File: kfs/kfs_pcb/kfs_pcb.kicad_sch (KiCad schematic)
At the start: 76 parts, among them SW0 SWITCH, SW1 SWITCH, SW10 SWITCH, SW11 SWITCH, SW12 SWITCH, SW13 SWITCH, SW14 SWITCH, SW15 SWITCH, SW16 SWITCH, SW17 SWITCH, SW18 SWITCH, SW19 SWITCH, SW2 SWITCH, SW20 SWITCH, SW21 SWITCH, SW22 SWITCH, SW23 SWITCH, SW24 SWITCH, SW25 SWITCH, SW26 SWITCH, SW27 SWITCH, SW28 SWITCH, SW29 SWITCH, SW3 SWITCH, SW30 SWITCH, SW31 SWITCH, SW32 SWITCH, SW33 SWITCH, SW34 SWITCH, SW35 SWITCH, SW36 SWITCH, SW37 SWITCH, SW38 SWITCH, SW39 SWITCH, SW4 SWITCH, SW40 SWITCH, SW41 SWITCH, SW42 SWITCH, SW43 SWITCH, SW44 SWITCH, SW45 SWITCH, SW46 SWITCH, SW47 SWITCH, SW48 SWITCH, SW49 SWITCH, SW5 SWITCH, SW50 SWITCH, SW51 SWITCH, SW52 SWITCH, SW53 SWITCH, SW54 SWITCH, SW55 SWITCH, SW56 SWITCH, SW57 SWITCH, SW58 SWITCH, SW59 SWITCH, SW6 SWITCH, SW60 SWITCH, SW61 SWITCH, SW62 SWITCH, SW63 SWITCH, SW7 SWITCH, SW8 SWITCH, SW9 SWITCH, U0 ARDUINO_PRO_MICRO

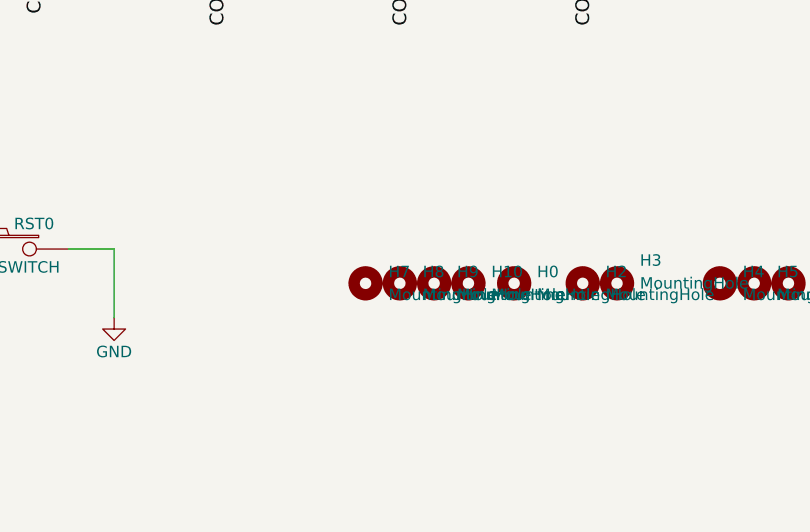
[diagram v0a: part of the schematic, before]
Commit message: Moved the bottom row of kfs farther inward.
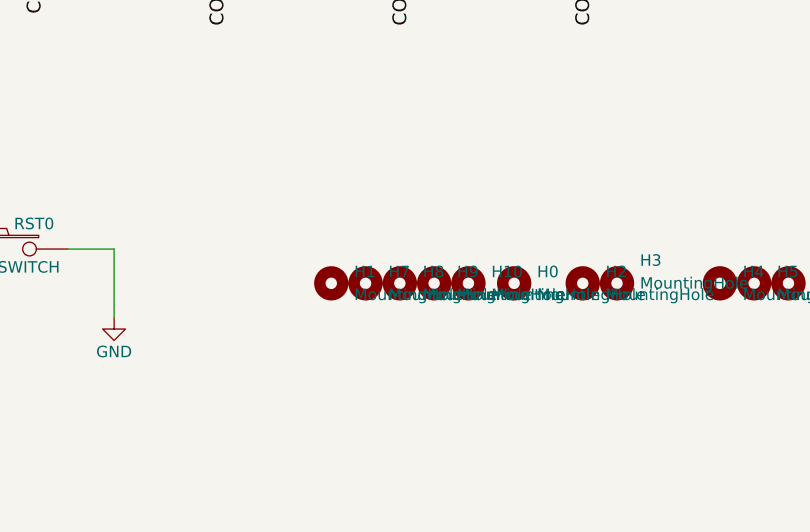
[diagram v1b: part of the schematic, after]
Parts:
- added H1: MountingHole, MountingHole:MountingHole_3.5mm, symbol Mechanical:MountingHole
- U0: footprint ProMicro_v2 -> footprints:ARDUINO_PRO_MICRO
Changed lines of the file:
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@@
       (effects (font (size 1.524 1.524)))
     )
-    (property "Footprint" "ProMicro_v2" (at 182.88 190.5 0)
+    (property "Footprint" "footprints:ARDUINO_PRO_MICRO" (at 182.88 190.5 0)
       (effects (font (size 1.524 1.524)) hide)
     )
@@
         )
       )
+    )
+  )
+  (symbol (lib_id "Mechanical:MountingHole") (at 250.19 153.67 0) (unit 1)
+    (in_bom yes) (on_board yes) (dnp no) (fields_autoplaced)
+    (property "Reference" "H1" (at 252.73 152.4 0)
+      (effects (font (size 1.27 1.27)) (justify left))
+    )
+    (property "Value" "MountingHole" (at 252.73 154.94 0)
+      (effects (font (size 1.27 1.27)) (justify left))
+    )
+    (property "Footprint" "MountingHole:MountingHole_3.5mm" (at 250.19 153.67 0)
+      (effects (font (size 1.27 1.27)) hide)
+    )
+    (property "Datasheet" "~" (at 250.19 153.67 0)
+      (effects (font (size 1.27 1.27)) hide)
+    )
+    (instances
+      (project "kfs_pcb"
+        (path "/97127b28-60f4-45ff-835e-dccfbc833331"
+          (reference "H1") (unit 1)
+        )
+      )

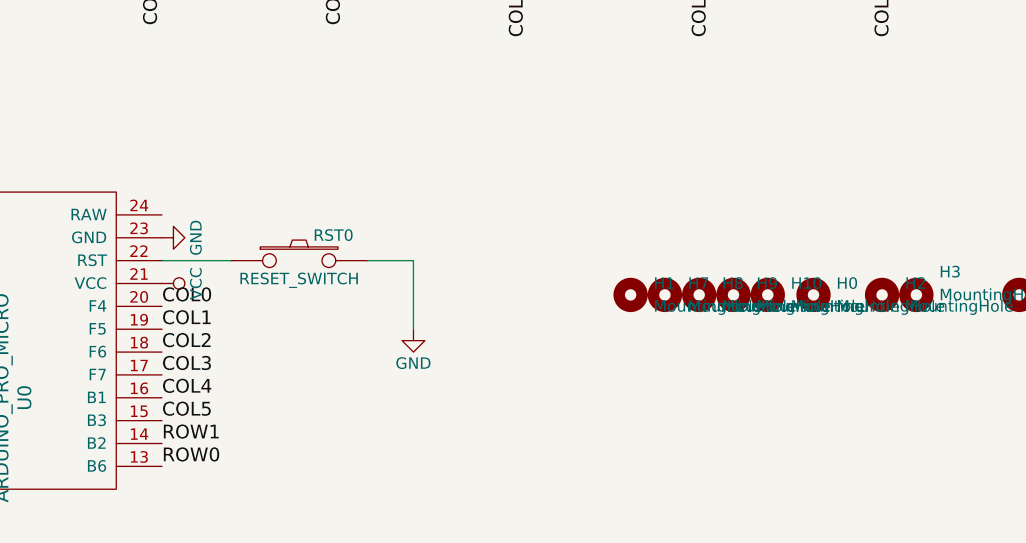
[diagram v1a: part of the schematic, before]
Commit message: Updated reset button and mounting holes on kfs.
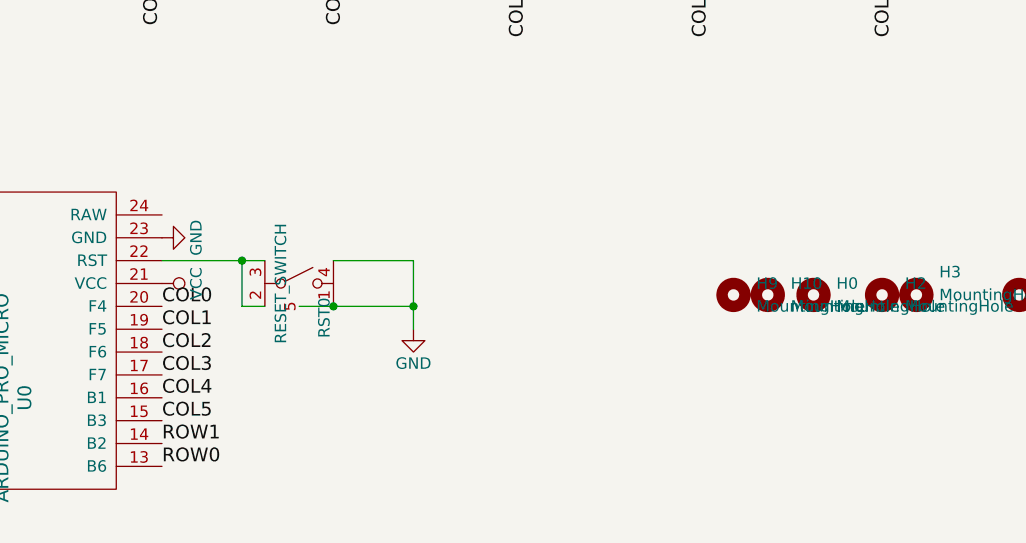
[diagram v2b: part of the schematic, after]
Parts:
- removed H1, H7, H8: MountingHole, MountingHole:MountingHole_3.5mm, symbol Mechanical:MountingHole
- RST0: footprint footprints:reset_button -> footprints:reset_button_1; symbol symbols:SWITCH_PUSH -> symbols:RESET_BUTTON
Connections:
- net GND: now also RST0.1, RST0.4, RST0.5; no longer RST0.2
- net at U0.22 (RST): now also RST0.2, RST0.3; no longer RST0.1
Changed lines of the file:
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@@
   (junction (at 193.04 35.56) (diameter 0) (color 0 0 0 0)
   )
+  (junction (at 217.17 154.94) (diameter 0) (color 0 0 0 0)
+  )
   (junction (at 91.44 92.71) (diameter 0) (color 0 0 0 0)
   )
@@
   (junction (at 152.4 111.76) (diameter 0) (color 0 0 0 0)
   )
+  (junction (at 207.01 149.86) (diameter 0) (color 0 0 0 0)
+  )
+  (junction (at 226.06 154.94) (diameter 0) (color 0 0 0 0)
+  )
   (junction (at 111.76 35.56) (diameter 0) (color 0 0 0 0)
   )
@@
     (stroke (width 0) (type default))
   )
+  (wire (pts (xy 226.06 154.94) (xy 226.06 157.48))
+    (stroke (width 0) (type default))
+  )
   (wire (pts (xy 55.88 27.94) (xy 55.88 46.99))
     (stroke (width 0) (type default))
@@
     (stroke (width 0) (type default))
   )
+  (wire (pts (xy 207.01 149.86) (xy 209.55 149.86))
+    (stroke (width 0) (type default))
+  )
   (wire (pts (xy 238.76 27.94) (xy 238.76 46.99))
     (stroke (width 0) (type default))
@@
     (stroke (width 0) (type default))
   )
-  (wire (pts (xy 226.06 149.86) (xy 226.06 157.48))
-    (stroke (width 0) (type default))
-  )
   (wire (pts (xy 152.4 35.56) (xy 172.72 35.56))
     (stroke (width 0) (type default))
@@
     (stroke (width 0) (type default))
   )
+  (wire (pts (xy 213.36 154.94) (xy 217.17 154.94))
+    (stroke (width 0) (type default))
+  )
   (wire (pts (xy 172.72 73.66) (xy 193.04 73.66))
     (stroke (width 0) (type default))
   )
+  (wire (pts (xy 209.55 154.94) (xy 207.01 154.94))
+    (stroke (width 0) (type default))
+  )
   (wire (pts (xy 238.76 85.09) (xy 238.76 104.14))
     (stroke (width 0) (type default))
   )
-  (wire (pts (xy 220.98 149.86) (xy 226.06 149.86))
+  (wire (pts (xy 217.17 149.86) (xy 226.06 149.86))
     (stroke (width 0) (type default))
   )
@@
     (stroke (width 0) (type default))
   )
-  (wire (pts (xy 198.12 149.86) (xy 205.74 149.86))
-    (stroke (width 0) (type default))
-  )
   (wire (pts (xy 254 111.76) (xy 274.32 111.76))
     (stroke (width 0) (type default))
@@
     (stroke (width 0) (type default))
   )
+  (wire (pts (xy 207.01 154.94) (xy 207.01 149.86))
+    (stroke (width 0) (type default))
+  )
   (wire (pts (xy 157.48 27.94) (xy 157.48 46.99))
     (stroke (width 0) (type default))
@@
     (stroke (width 0) (type default))
   )
+  (wire (pts (xy 217.17 154.94) (xy 226.06 154.94))
+    (stroke (width 0) (type default))
+  )
   (wire (pts (xy 111.76 54.61) (xy 132.08 54.61))
     (stroke (width 0) (type default))
@@
     (stroke (width 0) (type default))
   )
+  (wire (pts (xy 198.12 149.86) (xy 207.01 149.86))
+    (stroke (width 0) (type default))
+  )
   (wire (pts (xy 238.76 66.04) (xy 238.76 85.09))
     (stroke (width 0) (type default))
@@
   )
   (wire (pts (xy 193.04 54.61) (xy 213.36 54.61))
+    (stroke (width 0) (type default))
+  )
+  (wire (pts (xy 226.06 149.86) (xy 226.06 154.94))
     (stroke (width 0) (type default))
   )
@@
     )
   )
-  (symbol (lib_id "symbols:SWITCH_PUSH") (at 213.36 149.86 0) (unit 1)
+  (symbol (lib_id "symbols:RESET_BUTTON") (at 213.36 152.4 270) (unit 1)
     (in_bom yes) (on_board yes) (dnp no)
-    (property "Reference" "RST0" (at 217.17 147.066 0)
-      (effects (font (size 1.27 1.27)))
-    )
-    (property "Value" "RESET_SWITCH" (at 213.36 151.892 0)
-      (effects (font (size 1.27 1.27)))
-    )
-    (property "Footprint" "footprints:reset_button" (at 213.36 149.86 0)
-      (effects (font (size 1.524 1.524)) hide)
-    )
-    (property "Datasheet" "" (at 213.36 149.86 0)
-      (effects (font (size 1.524 1.524)) hide)
-    )
-    (pin "1")
-    (pin "2")
+    (property "Reference" "RST0" (at 216.154 156.21 0)
+      (effects (font (size 1.27 1.27)))
+    )
+    (property "Value" "RESET_SWITCH" (at 211.328 152.4 0)
+      (effects (font (size 1.27 1.27)))
+    )
+    (property "Footprint" "footprints:reset_button_1" (at 213.36 152.4 90)
+      (effects (font (size 1.27 1.27)) hide)
+    )
+    (property "Datasheet" "" (at 213.36 152.4 90)
+      (effects (font (size 1.27 1.27)) hide)
+    )
+    (pin "1")
+    (pin "2")
+    (pin "4")
+    (pin "5")
+    (pin "3")
     (instances
       (project "kfs_pcb"
@@
     )
   )
-  (symbol (lib_id "Mechanical:MountingHole") (at 250.19 153.67 0) (unit 1)
-    (in_bom yes) (on_board yes) (dnp no) (fields_autoplaced)
-    (property "Reference" "H1" (at 252.73 152.4 0)
-      (effects (font (size 1.27 1.27)) (justify left))
-    )
-    (property "Value" "MountingHole" (at 252.73 154.94 0)
-      (effects (font (size 1.27 1.27)) (justify left))
-    )
-    (property "Footprint" "MountingHole:MountingHole_3.5mm" (at 250.19 153.67 0)
-      (effects (font (size 1.27 1.27)) hide)
-    )
-    (property "Datasheet" "~" (at 250.19 153.67 0)
-      (effects (font (size 1.27 1.27)) hide)
-    )
-    (instances
-      (project "kfs_pcb"
-        (path "/97127b28-60f4-45ff-835e-dccfbc833331"
-          (reference "H1") (unit 1)
-        )
-      )
-    )
-  )
   (symbol (lib_id "symbols:SWITCH_WITH_DIODE") (at 226.06 66.04 0) (unit 1)
     (in_bom yes) (on_board yes) (dnp no) (fields_autoplaced)
@@
     )
   )
-  (symbol (lib_id "Mechanical:MountingHole") (at 254 153.67 0) (unit 1)
-    (in_bom yes) (on_board yes) (dnp no) (fields_autoplaced)
-    (property "Reference" "H7" (at 256.54 152.4 0)
-      (effects (font (size 1.27 1.27)) (justify left))
-    )
-    (property "Value" "MountingHole" (at 256.54 154.94 0)
-      (effects (font (size 1.27 1.27)) (justify left))
-    )
-    (property "Footprint" "MountingHole:MountingHole_3.5mm" (at 254 153.67 0)
-      (effects (font (size 1.27 1.27)) hide)
-    )
-    (property "Datasheet" "~" (at 254 153.67 0)
-      (effects (font (size 1.27 1.27)) hide)
-    )
-    (instances
-      (project "kfs_pcb"
-        (path "/97127b28-60f4-45ff-835e-dccfbc833331"
-          (reference "H7") (unit 1)
-        )
-      )
-    )
-  )
   (symbol (lib_id "symbols:SWITCH_WITH_DIODE") (at 226.06 46.99 0) (unit 1)
     (in_bom yes) (on_board yes) (dnp no) (fields_autoplaced)
@@
         )
       )
-    )
-  )
-  (symbol (lib_id "Mechanical:MountingHole") (at 257.81 153.67 0) (unit 1)
-    (in_bom yes) (on_board yes) (dnp no) (fields_autoplaced)
-    (property "Reference" "H8" (at 260.35 152.4 0)
-      (effects (font (size 1.27 1.27)) (justify left))
-    )
-    (property "Value" "MountingHole" (at 260.35 154.94 0)
-      (effects (font (size 1.27 1.27)) (justify left))
-    )
-    (property "Footprint" "MountingHole:MountingHole_3.5mm" (at 257.81 153.67 0)
-      (effects (font (size 1.27 1.27)) hide)
-    )
-    (property "Datasheet" "~" (at 257.81 153.67 0)
-      (effects (font (size 1.27 1.27)) hide)
-    )
-    (instances
-      (project "kfs_pcb"
-        (path "/97127b28-60f4-45ff-835e-dccfbc833331"
-          (reference "H8") (unit 1)
-        )
-      )

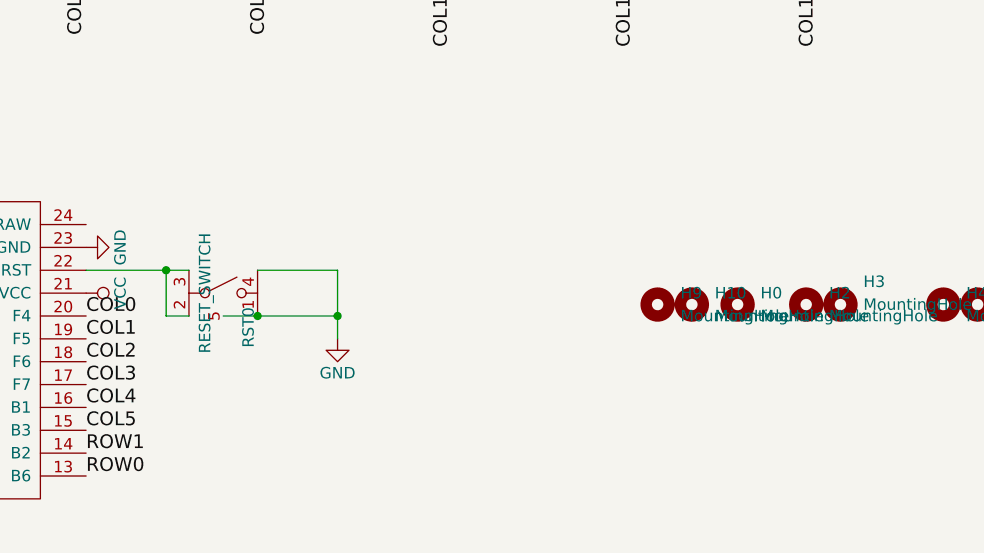
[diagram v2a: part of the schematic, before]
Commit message: Changed reset button again. Removed some standoffs.
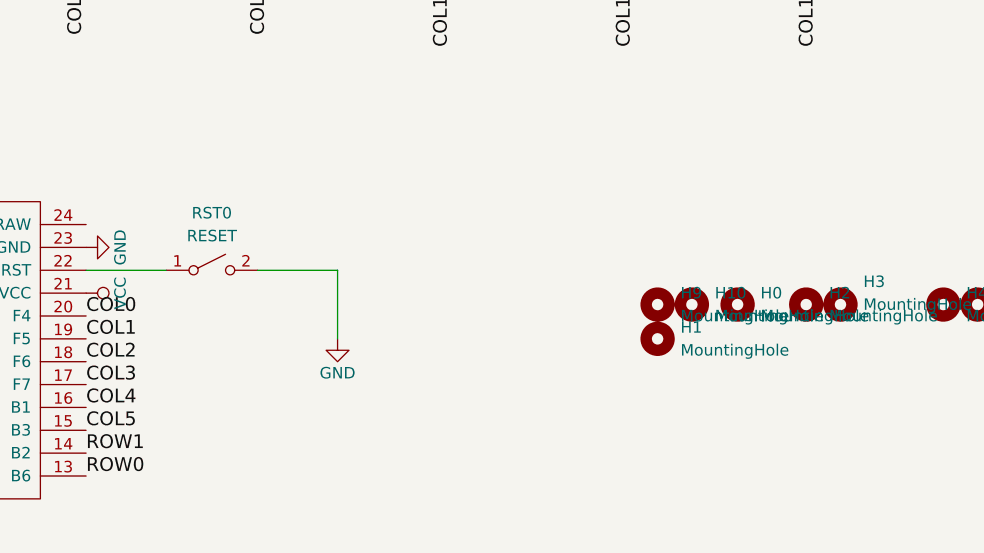
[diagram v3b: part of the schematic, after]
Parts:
- removed RST0: RESET_SWITCH, footprints:reset_button_1, symbol symbols:RESET_BUTTON
- added H1: MountingHole, MountingHole:MountingHole_3.5mm, symbol Mechanical:MountingHole
- added RST0: RESET, footprints:reset_button_1, symbol Switch:SW_SPST
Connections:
- net GND: now also RST0.2 (B)
- net at U0.22 (RST): now also RST0.1 (A)
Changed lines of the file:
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@@
   (junction (at 193.04 35.56) (diameter 0) (color 0 0 0 0)
   )
-  (junction (at 217.17 154.94) (diameter 0) (color 0 0 0 0)
-  )
   (junction (at 91.44 92.71) (diameter 0) (color 0 0 0 0)
   )
@@
   (junction (at 152.4 111.76) (diameter 0) (color 0 0 0 0)
   )
-  (junction (at 207.01 149.86) (diameter 0) (color 0 0 0 0)
-  )
-  (junction (at 226.06 154.94) (diameter 0) (color 0 0 0 0)
-  )
   (junction (at 111.76 35.56) (diameter 0) (color 0 0 0 0)
   )
@@
     (stroke (width 0) (type default))
   )
-  (wire (pts (xy 226.06 154.94) (xy 226.06 157.48))
+  (wire (pts (xy 226.06 149.86) (xy 226.06 157.48))
     (stroke (width 0) (type default))
   )
@@
     (stroke (width 0) (type default))
   )
-  (wire (pts (xy 207.01 149.86) (xy 209.55 149.86))
-    (stroke (width 0) (type default))
-  )
   (wire (pts (xy 238.76 27.94) (xy 238.76 46.99))
     (stroke (width 0) (type default))
@@
     (stroke (width 0) (type default))
   )
-  (wire (pts (xy 213.36 154.94) (xy 217.17 154.94))
-    (stroke (width 0) (type default))
-  )
   (wire (pts (xy 172.72 73.66) (xy 193.04 73.66))
     (stroke (width 0) (type default))
   )
-  (wire (pts (xy 209.55 154.94) (xy 207.01 154.94))
-    (stroke (width 0) (type default))
-  )
   (wire (pts (xy 238.76 85.09) (xy 238.76 104.14))
     (stroke (width 0) (type default))
@@
     (stroke (width 0) (type default))
   )
+  (wire (pts (xy 198.12 149.86) (xy 207.01 149.86))
+    (stroke (width 0) (type default))
+  )
   (wire (pts (xy 274.32 54.61) (xy 294.64 54.61))
     (stroke (width 0) (type default))
@@
     (stroke (width 0) (type default))
   )
-  (wire (pts (xy 207.01 154.94) (xy 207.01 149.86))
-    (stroke (width 0) (type default))
-  )
   (wire (pts (xy 157.48 27.94) (xy 157.48 46.99))
     (stroke (width 0) (type default))
@@
     (stroke (width 0) (type default))
   )
-  (wire (pts (xy 217.17 154.94) (xy 226.06 154.94))
-    (stroke (width 0) (type default))
-  )
   (wire (pts (xy 111.76 54.61) (xy 132.08 54.61))
     (stroke (width 0) (type default))
@@
     (stroke (width 0) (type default))
   )
-  (wire (pts (xy 198.12 149.86) (xy 207.01 149.86))
-    (stroke (width 0) (type default))
-  )
   (wire (pts (xy 238.76 66.04) (xy 238.76 85.09))
     (stroke (width 0) (type default))
@@
   )
   (wire (pts (xy 193.04 54.61) (xy 213.36 54.61))
-    (stroke (width 0) (type default))
-  )
-  (wire (pts (xy 226.06 149.86) (xy 226.06 154.94))
     (stroke (width 0) (type default))
   )
@@
     )
   )
-  (symbol (lib_id "symbols:RESET_BUTTON") (at 213.36 152.4 270) (unit 1)
-    (in_bom yes) (on_board yes) (dnp no)
-    (property "Reference" "RST0" (at 216.154 156.21 0)
-      (effects (font (size 1.27 1.27)))
-    )
-    (property "Value" "RESET_SWITCH" (at 211.328 152.4 0)
-      (effects (font (size 1.27 1.27)))
-    )
-    (property "Footprint" "footprints:reset_button_1" (at 213.36 152.4 90)
-      (effects (font (size 1.27 1.27)) hide)
-    )
-    (property "Datasheet" "" (at 213.36 152.4 90)
-      (effects (font (size 1.27 1.27)) hide)
-    )
-    (pin "1")
-    (pin "2")
-    (pin "4")
-    (pin "5")
-    (pin "3")
-    (instances
-      (project "kfs_pcb"
-        (path "/97127b28-60f4-45ff-835e-dccfbc833331"
-          (reference "RST0") (unit 1)
-        )
-      )
-    )
-  )
   (symbol (lib_id "Atreus62-rescue:GND") (at 226.06 157.48 0) (unit 1)
     (in_bom yes) (on_board yes) (dnp no)
@@
         (path "/97127b28-60f4-45ff-835e-dccfbc833331"
           (reference "SW52") (unit 1)
+        )
+      )
+    )
+  )
+  (symbol (lib_id "Mechanical:MountingHole") (at 261.62 157.48 0) (unit 1)
+    (in_bom yes) (on_board yes) (dnp no) (fields_autoplaced)
+    (property "Reference" "H1" (at 264.16 156.21 0)
+      (effects (font (size 1.27 1.27)) (justify left))
+    )
+    (property "Value" "MountingHole" (at 264.16 158.75 0)
+      (effects (font (size 1.27 1.27)) (justify left))
+    )
+    (property "Footprint" "MountingHole:MountingHole_3.5mm" (at 261.62 157.48 0)
+      (effects (font (size 1.27 1.27)) hide)
+    )
+    (property "Datasheet" "~" (at 261.62 157.48 0)
+      (effects (font (size 1.27 1.27)) hide)
+    )
+    (instances
+      (project "kfs_pcb"
+        (path "/97127b28-60f4-45ff-835e-dccfbc833331"
+          (reference "H1") (unit 1)
         )
       )
@@
         )
       )
+    )
+  )
+  (symbol (lib_id "Switch:SW_SPST") (at 212.09 149.86 0) (unit 1)
+    (in_bom yes) (on_board yes) (dnp no) (fields_autoplaced)
+    (property "Reference" "RST0" (at 212.09 143.51 0)
+      (effects (font (size 1.27 1.27)))
+    )
+    (property "Value" "RESET" (at 212.09 146.05 0)
+      (effects (font (size 1.27 1.27)))
+    )
+    (property "Footprint" "footprints:reset_button_1" (at 212.09 149.86 0)
+      (effects (font (size 1.27 1.27)) hide)
+    )
+    (property "Datasheet" "~" (at 212.09 149.86 0)
+      (effects (font (size 1.27 1.27)) hide)
+    )
+    (pin "2")
+    (pin "1")
+    (instances
+      (project "kfs_pcb"
+        (path "/97127b28-60f4-45ff-835e-dccfbc833331"
+          (reference "RST0") (unit 1)
+        )
+      )
